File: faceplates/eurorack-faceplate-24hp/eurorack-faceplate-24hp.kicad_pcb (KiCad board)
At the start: 2 copper layers, 121.6 x 133.3 mm, 4 parts

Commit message: Moving mounting holes
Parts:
- moved REF** 2.42 mm to (5.08, 130.3)
- moved REF** 2.42 mm to (5.08, 3.00)
- moved REF** 2.34 mm to (116.5, 130.3)
- moved REF** 2.34 mm to (116.5, 3.00)
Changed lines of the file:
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@@
   (net 0 "")
   (footprint "MountingHole:MountingHole_3.2mm_M3" (layer "F.Cu")
-    (at 7.5 130.35)
+    (at 5.08 130.35)
     (descr "Mounting Hole 3.2mm, no annular, M3")
     (tags "mounting hole 3.2mm no annular m3")
@@
   )
   (footprint "MountingHole:MountingHole_3.2mm_M3" (layer "F.Cu")
-    (at 114.18 130.35)
+    (at 116.52 130.35)
     (descr "Mounting Hole 3.2mm, no annular, M3")
     (tags "mounting hole 3.2mm no annular m3")
@@
   )
   (footprint "MountingHole:MountingHole_3.2mm_M3" (layer "F.Cu")
-    (at 114.18 3)
+    (at 116.52 3)
     (descr "Mounting Hole 3.2mm, no annular, M3")
     (tags "mounting hole 3.2mm no annular m3")
@@
   )
   (footprint "MountingHole:MountingHole_3.2mm_M3" (layer "F.Cu")
-    (at 7.5 3)
+    (at 5.08 3)
     (descr "Mounting Hole 3.2mm, no annular, M3")
     (tags "mounting hole 3.2mm no annular m3")
@@
   (gr_line (start 0 0) (end 121.6 0) (layer "Edge.Cuts") (width 0.1))
   (gr_line (start 121.6 133.35) (end 0 133.35) (layer "Edge.Cuts") (width 0.1))
+  (dimension (type aligned) (layer "User.1")
+    (pts (xy 5.08 3) (xy 0 3))
+    (height 7)
+    (gr_text "5.0800 mm" (at 2.54 -5.15) (layer "User.1")
+      (effects (font (size 1 1) (thickness 0.15)))
+    )
+    (format (units 3) (units_format 1) (precision 4))
+    (style (thickness 0.15) (arrow_length 1.27) (text_position_mode 0) (extension_height 0.58642) (extension_offset 0.5) keep_text_aligned)
+  )
 )

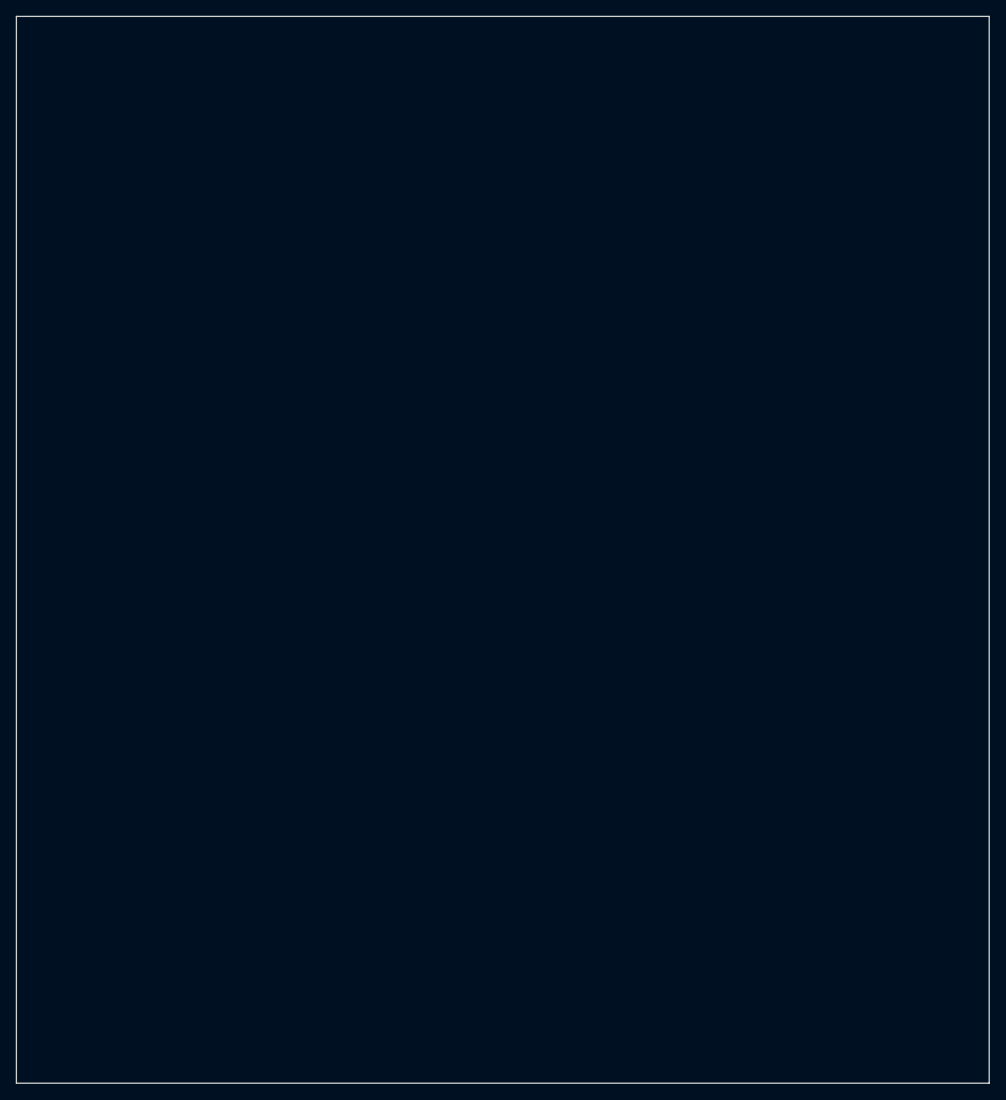
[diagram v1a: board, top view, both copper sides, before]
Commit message: Correcting panel height
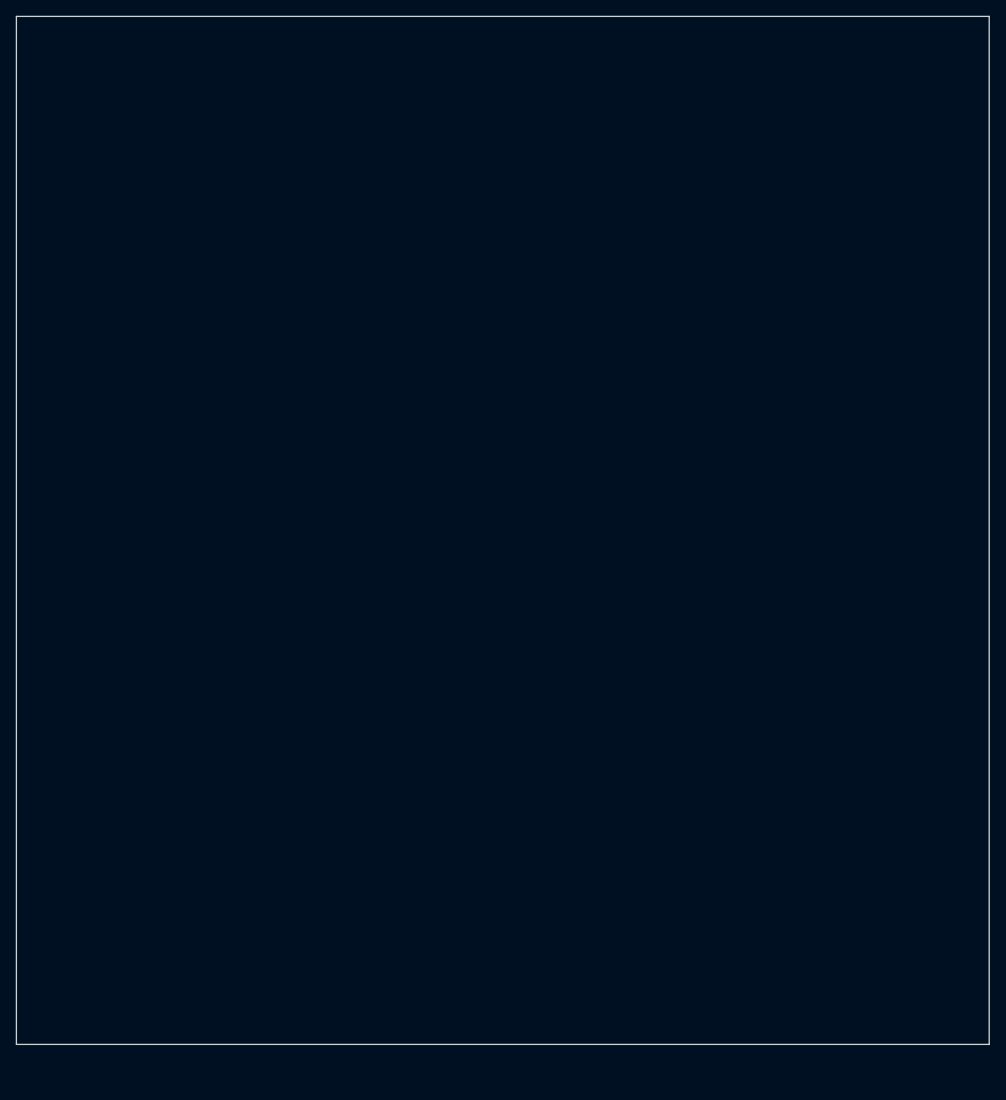
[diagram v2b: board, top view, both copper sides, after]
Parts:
- moved REF** 4.85 mm to (5.08, 125.5)
- moved REF** 4.85 mm to (116.5, 125.5)
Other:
- board size 121.6 x 133.3 mm -> 121.6 x 128.5 mm
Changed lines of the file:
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@@
   (net 0 "")
   (footprint "MountingHole:MountingHole_3.2mm_M3" (layer "F.Cu")
-    (at 5.08 130.35)
+    (at 5.08 125.5)
     (descr "Mounting Hole 3.2mm, no annular, M3")
     (tags "mounting hole 3.2mm no annular m3")
@@
   )
   (footprint "MountingHole:MountingHole_3.2mm_M3" (layer "F.Cu")
-    (at 116.52 130.35)
+    (at 116.52 125.5)
     (descr "Mounting Hole 3.2mm, no annular, M3")
     (tags "mounting hole 3.2mm no annular m3")
@@
     (pad "" np_thru_hole oval locked (at 0 0) (size 7 3.2) (drill oval 7 3.2) (layers F&B.Cu *.Mask))
   )
-  (gr_line (start 121.6 0) (end 121.6 133.35) (layer "Edge.Cuts") (width 0.1))
-  (gr_line (start 0 133.35) (end 0 0) (layer "Edge.Cuts") (width 0.1))
+  (gr_line (start 121.6 0) (end 121.6 128.5) (layer "Edge.Cuts") (width 0.1))
+  (gr_line (start 0 128.5) (end 0 0) (layer "Edge.Cuts") (width 0.1))
   (gr_line (start 0 0) (end 121.6 0) (layer "Edge.Cuts") (width 0.1))
-  (gr_line (start 121.6 133.35) (end 0 133.35) (layer "Edge.Cuts") (width 0.1))
+  (gr_line (start 121.6 128.5) (end 0 128.5) (layer "Edge.Cuts") (width 0.1))
   (dimension (type aligned) (layer "User.1")
     (pts (xy 5.08 3) (xy 0 3))
